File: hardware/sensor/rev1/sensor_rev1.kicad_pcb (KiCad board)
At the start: 2 copper layers, 28.9 x 64.4 mm, 58 parts, among them IC1 STM8L051F3P6, IC2 CC1101RGPR, J1 22-28-4044, J2 M20-9770342, Y1 NX3225GA-26.000M-STD-CRG-2

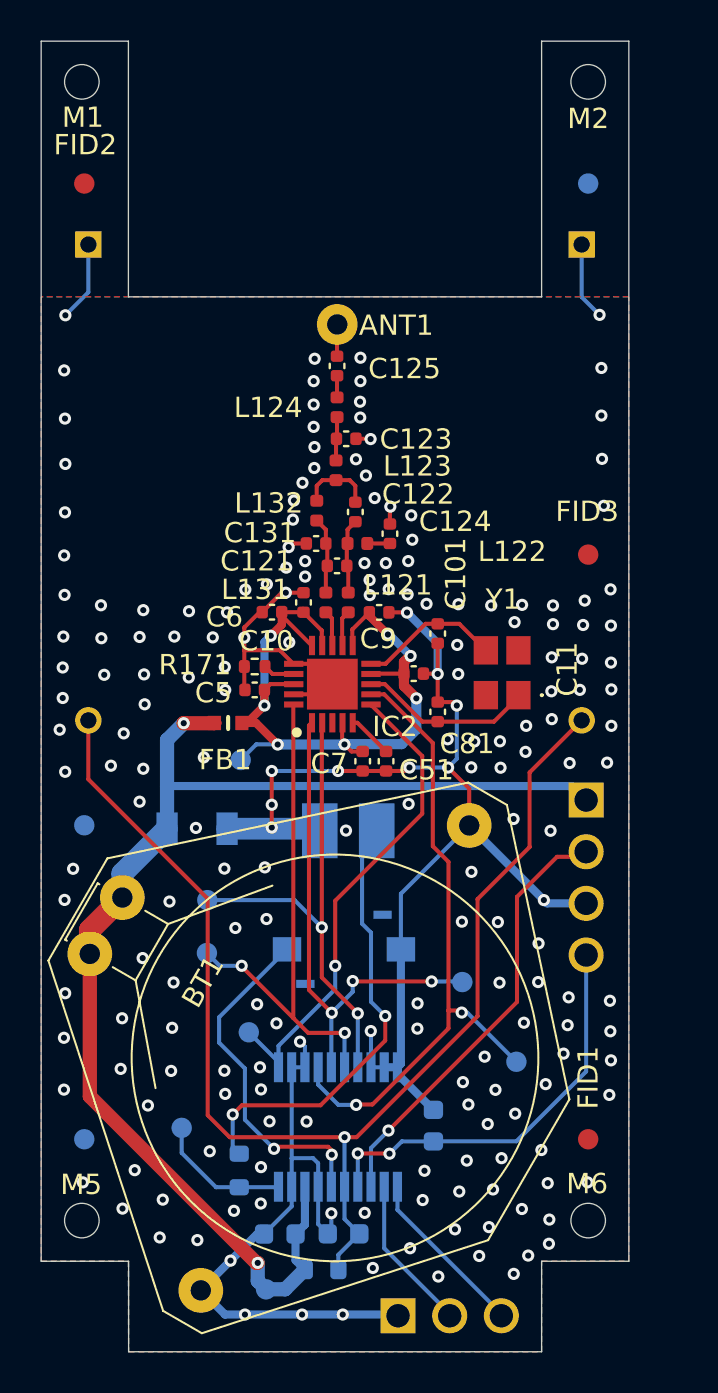
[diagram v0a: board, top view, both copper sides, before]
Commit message: EG-50 Fixes from new DRC rules (JLBPCB)
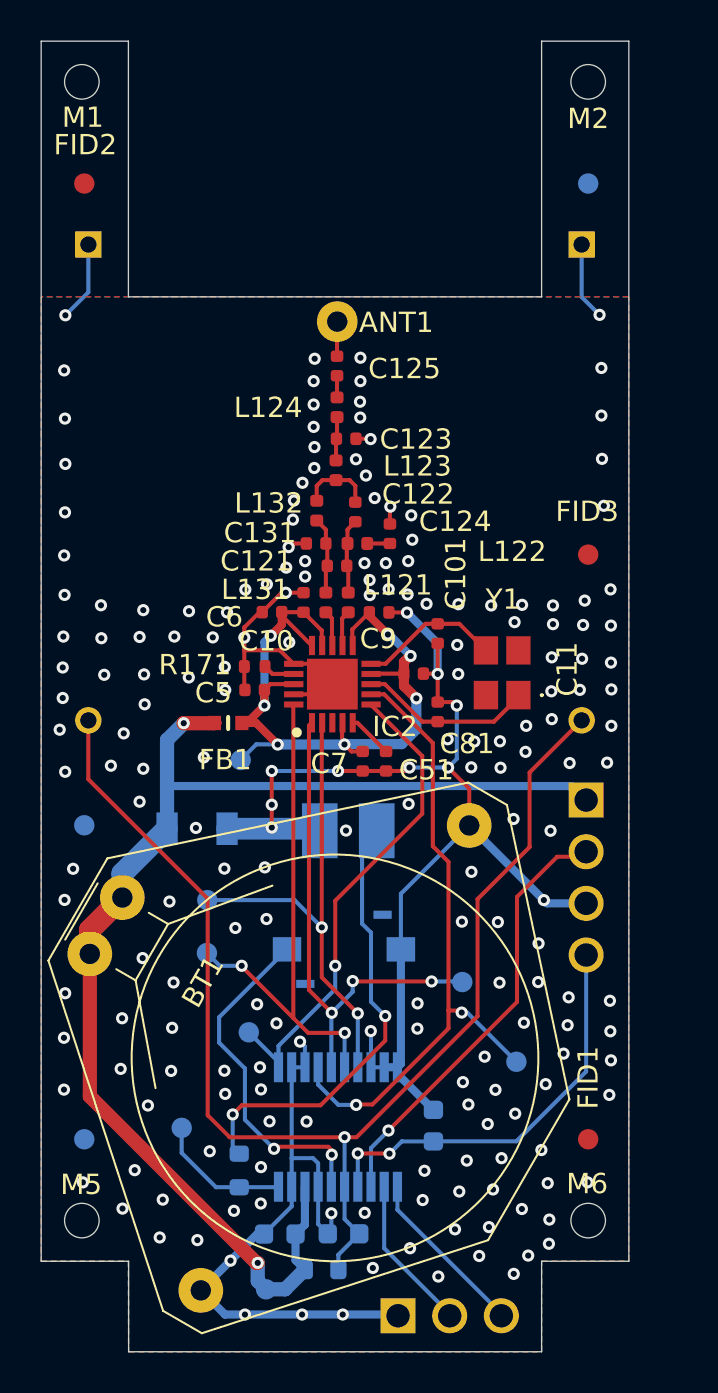
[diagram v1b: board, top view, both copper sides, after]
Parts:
- moved ANT1 0.14 mm to (234.5, 105.6)

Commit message: EG-70 All components in one face.
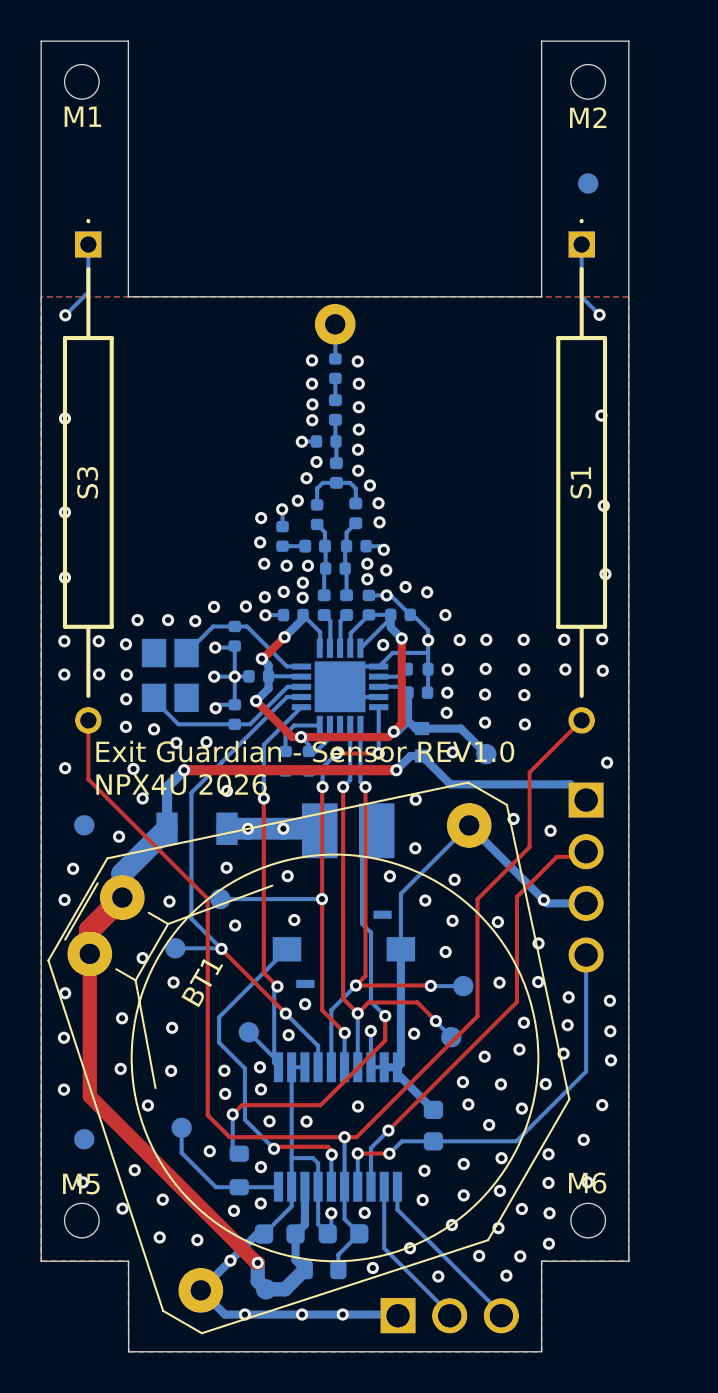
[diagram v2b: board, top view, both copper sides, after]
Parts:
- removed FID1, FID2, FID3: Fiducial, Fiducial:Fiducial_1mm_Mask2mm
- ANT1, C10, C101, C11, C121, C122, C123, C124, C125, C131, C5, C51, C6, C7, C81, C9, FB1, IC2, L121, L122, L123, L124, L131, L132, R171, Y1: moved to B.Cu
- S1, S3: moved to F.Cu
- moved CS1 17.7 mm to (226.6, 134.6)
- moved Y1 16.3 mm to (226.3, 121.2)
- moved MISO1 13.8 mm to (240.2, 139.0)
- moved RFVDD1 12.1 mm to (241.9, 125.1)
- moved C101 9.98 mm to (229.5, 119.3)
- moved C81 9.98 mm to (229.5, 123.1)
- moved FB1 9.58 mm to (238.7, 124.5), turned to -90 degrees
- moved C5 8.02 mm to (238.5, 122.0), turned to 0 degrees
- moved R171 8.02 mm to (238.5, 120.9), turned to 0 degrees
- moved C11 7.62 mm to (230.7, 121.2), turned to 180 degrees
- moved C6 6.32 mm to (237.7, 118.2), turned to 0 degrees
- moved C124 5.28 mm to (231.9, 114.4)
- moved C51 4.94 mm to (232.0, 125.4)
- moved C9 4.22 mm to (232.4, 118.2), turned to 180 degrees
- moved C10 3.22 mm to (236.1, 117.7)
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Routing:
- net GND: track 117.5 -> 97.7 mm, vias 203 -> 186
- net /MCU/CS: track 32.0 -> 25.7 mm
- net VDD: track 62.6 -> 58.8 mm, vias 2 -> 3
- net /MCU/IRQ: track 24.2 -> 21.3 mm, vias 1 -> 2
- net /MCU/SCLK: track 24.9 -> 22.9 mm
- net RF_VDD: track 38.6 -> 39.7 mm, vias 7 -> 6
- net /MCU/SDO: track 23.9 -> 22.9 mm, vias 2 -> 3
- net /MCU/SDI: track 25.5 -> 25.8 mm, vias 2 -> 5

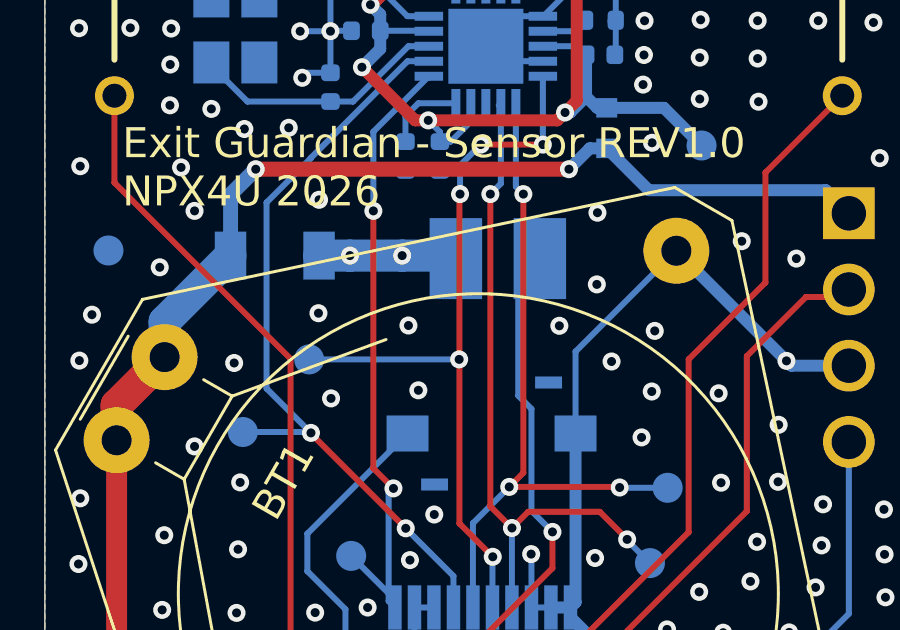
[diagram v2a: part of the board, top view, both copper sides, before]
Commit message: EG-70 Updated the LED from JLCPCB library.
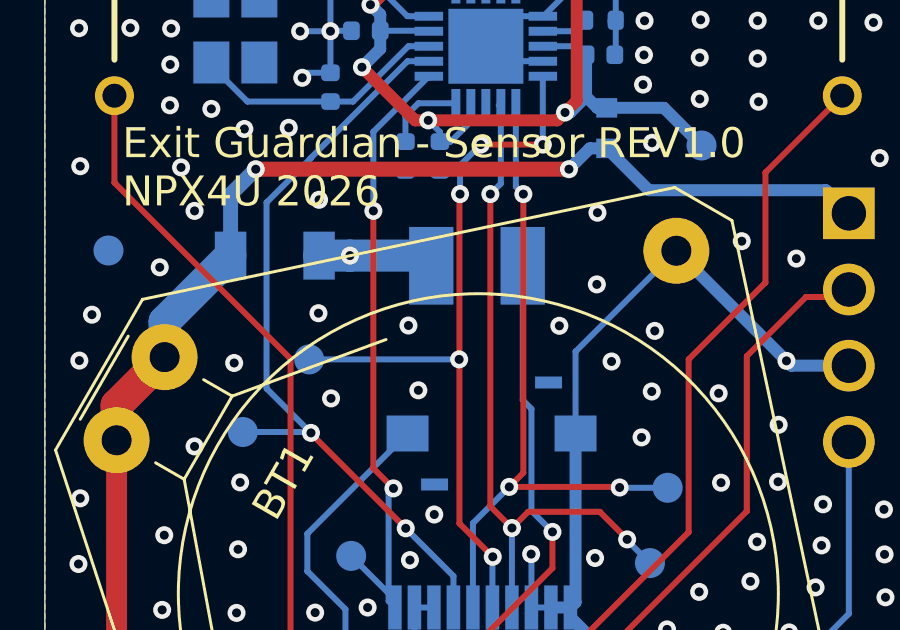
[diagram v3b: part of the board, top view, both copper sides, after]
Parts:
- removed LED1: VLMS3000-GS08, MyParts:VLMS3000GS08
- added D1: LED, MyParts:645-597-3008-207F, B.Cu at (234.4, 129.1)
- R1: value 100 -> 120
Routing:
- net GND: track 97.7 -> 96.9 mm, vias 186 -> 185
- net Net-(D1-A): track 22.2 -> 21.6 mm

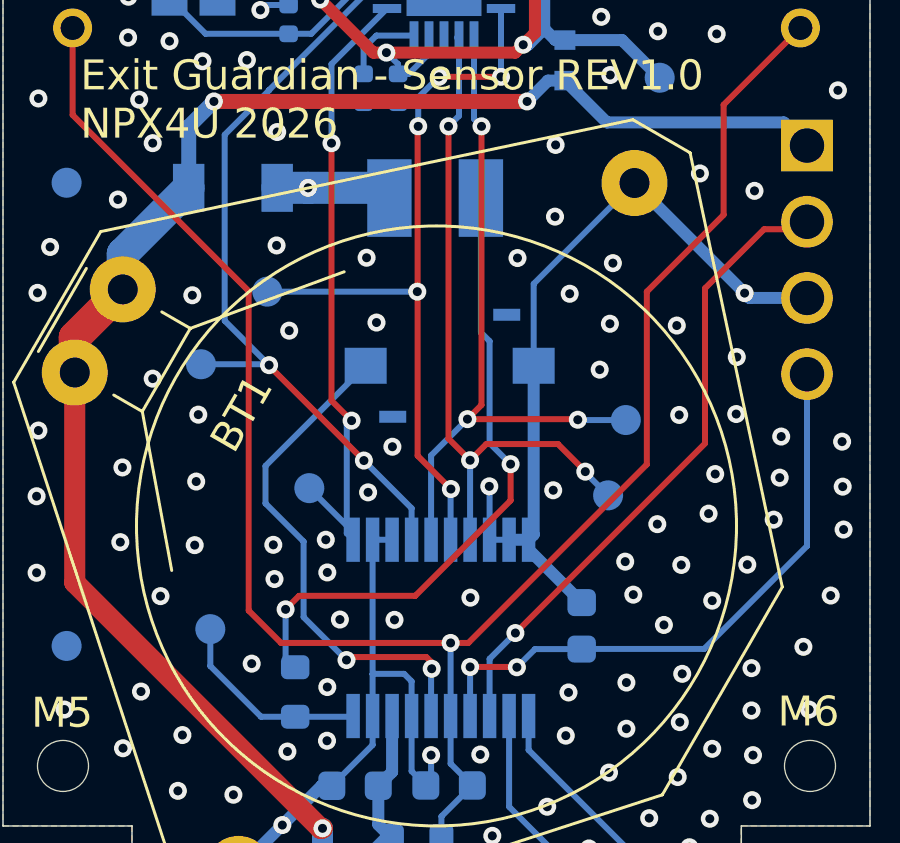
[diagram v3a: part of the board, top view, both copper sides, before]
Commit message: EG-70 Adaptions according with JLCPCB production constraints.
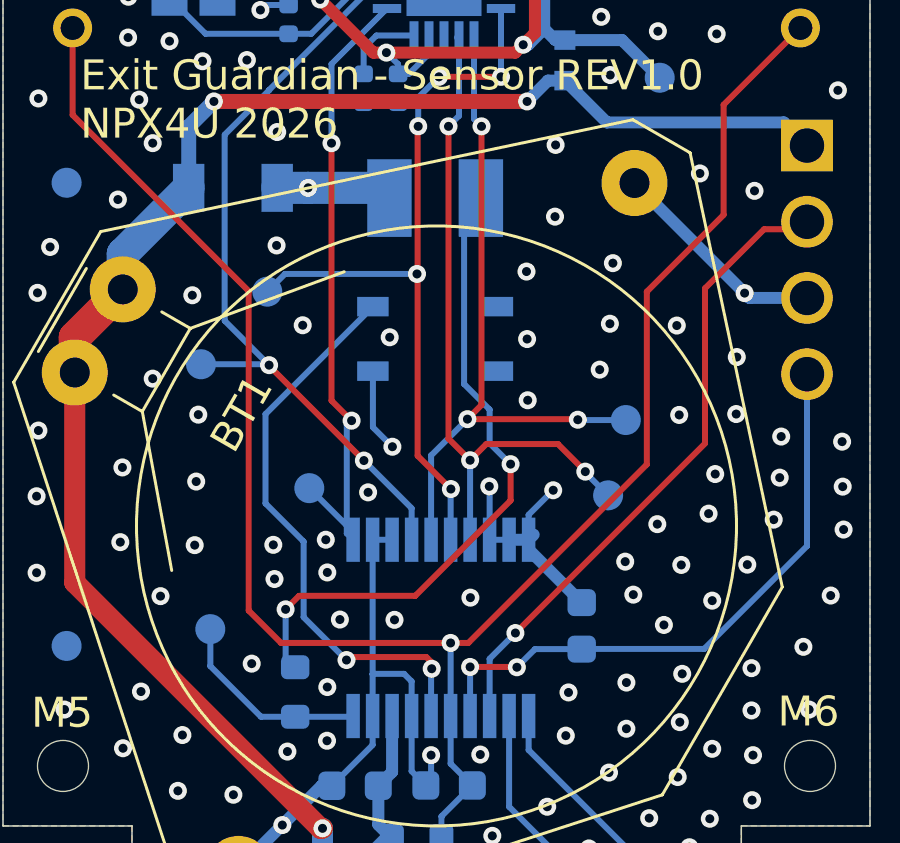
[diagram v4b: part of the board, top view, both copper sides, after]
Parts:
- S2: value PTS636SMG25JSMTR_LFS -> PTS810SJK250SMTR_LFS; footprint MyParts:PTS636SMG25JSMTRLFS -> MyParts:PTS810SJK250SMTRLFS
- moved S2 1.02 mm to (234.4, 133.8), turned to 180 degrees
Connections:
- S2 pad 1: BTN -> unconnected-(S2-NO_1-Pad1)
- S2 pad 2: GND -> BTN
- S2 pad 4: unconnected-(S2-GND_2-Pad4) -> GND
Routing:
- net GND: track 96.9 -> 88.6 mm
- net BTN: track 17.1 -> 19.1 mm

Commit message: EG-70 XTAL replaced according with JLCPCB constraints and capacitors adjusted accordingly.
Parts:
- C101, C81: value 12pF -> 15pF
- Y1: value NX3225GA-26.000M-STD-CRG-2 -> CG01972-26M
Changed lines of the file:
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@@
 			)
 		)
-		(property "Value" "NX3225GA-26.000M-STD-CRG-2"
+		(property "Value" "CG01972-26M"
 			(at 0 0 90)
 			(layer "B.SilkS")
@@
 			)
 		)
-		(property "Mouser Part Number" "344-NX3225GA26MSTRG2"
+		(property "Mouser Part Number" "344-NX3225GA26MHZTI"
 			(at 0 0 270)
 			(unlocked yes)
@@
 			)
 		)
-		(property "Manufacturer Part Number" "NX3225GA-26.000M-STD-CRG-2"
+		(property "Manufacturer Part Number" "CG01972-26M"
 			(at 0 0 270)
 			(unlocked yes)
@@
 			)
 		)
-		(property "Mouser Price/Stock" "https://www.mouser.co.uk/ProductDetail/NDK/NX3225GA-26.000M-STD-CRG-2?qs=w%2Fv1CP2dgqrNyFiUoufKQw%3D%3D"
+		(property "Mouser Price/Stock" "https://pt.mouser.com/en/ProductDetail/NDK/CG01972-26M?qs=Tc%252BHE9vUsntpTnxiVVqD7w%3D%3D"
 			(at 0 0 90)
 			(unlocked yes)
@@
 			)
 		)
-		(property "Value" "12pF"
+		(property "Value" "15pF"
 			(at -1.97 -1.45 90)
 			(layer "B.Fab")
@@
 			)
 		)
-		(property "Mouser Part Number" "81-GRM1555C1H120FA1D"
+		(property "Mouser Part Number" "77-VJ0402D150FXCAJ"
 			(at 0 0 270)
 			(unlocked yes)
@@
 			)
 		)
-		(property "Mouser Price/Stock" "https://pt.mouser.com/ProductDetail/Murata-Electronics/GRM1555C1H120FA01D?qs=ouTquLLW2S4GiX6b03cbUg%3D%3D"
+		(property "Mouser Price/Stock" "https://pt.mouser.com/en/ProductDetail/Vishay-Vitramon/VJ0402D150FXCAJ?qs=iYZfuFMDqcZeWrff4BZNMQ%3D%3D"
 			(at 0 0 270)
 			(unlocked yes)
@@
 			)
 		)
-		(property "Manufacturer_Name" "Murata Electronics"
+		(property "Manufacturer_Name" "Vishay"
 			(at 0 0 270)
 			(unlocked yes)
@@
 			)
 		)
-		(property "Manufacturer_Part_Number" "GRM1555C1H120FA1D"
+		(property "Manufacturer_Part_Number" "VJ0402D150FXCAJ"
 			(at 0 0 270)
 			(unlocked yes)
@@
 			)
 		)
-		(property "Manufacturer_Part_Number" "597-3008-207F "
+		(property "Manufacturer_Part_Number" "5973008207F "
 			(at 0 0 270)
 			(unlocked yes)
@@
 			)
 		)
-		(property "Value" "12pF"
+		(property "Value" "15pF"
 			(at -2.23 1.25 90)
 			(layer "B.Fab")
@@
 			)
 		)
-		(property "Mouser Part Number" "81-GRM1555C1H120FA1D"
+		(property "Mouser Part Number" "77-VJ0402D150FXCAJ"
 			(at 0 0 90)
 			(unlocked yes)
@@
 			)
 		)
-		(property "Manufacturer_Name" "Murata Electronics"
+		(property "Manufacturer_Name" "Vishay"
 			(at 0 0 90)
 			(unlocked yes)
@@
 			)
 		)
-		(property "Manufacturer_Part_Number" "GRM1555C1H120FA1D"
+		(property "Manufacturer_Part_Number" "VJ0402D150FXCAJ"
 			(at 0 0 90)
 			(unlocked yes)

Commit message: EG-70 Adaptions on XTAL name.
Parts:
- Y1: value CG01972-26M -> NX3225GA-26MHZ-TI
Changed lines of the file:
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@@
 			)
 		)
-		(property "Value" "CG01972-26M"
+		(property "Value" "NX3225GA-26MHZ-TI"
 			(at 0 0 90)
 			(layer "B.SilkS")
@@
 			)
 		)
-		(property "Manufacturer Part Number" "CG01972-26M"
+		(property "Manufacturer Part Number" "NX3225GA-26MHZ-TI"
 			(at 0 0 270)
 			(unlocked yes)

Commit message: EG-70 Delete components from BOM and position file.
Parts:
- D1: value LED -> 597-3008-207F
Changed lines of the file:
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@@
 			)
 		)
-		(property "Value" "LED"
+		(property "Value" "597-3008-207F"
 			(at 0 -1 90)
 			(unlocked yes)
@@
 			)
 		)
-		(property "Manufacturer_Part_Number" "5973008207F "
+		(property "Manufacturer_Part_Number" "597-3008-207F"
 			(at 0 0 270)
 			(unlocked yes)
